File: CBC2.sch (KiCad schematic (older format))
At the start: 204 parts, among them K0:0 KEYSW, K0:1 KEYSW, K0:10 KEYSW, K0:11 KEYSW, K0:12 KEYSW, K0:13 KEYSW, K0:14 KEYSW, K0:15 KEYSW, K0:16 KEYSW, K0:2 KEYSW, K0:3 KEYSW, K0:4 KEYSW, K0:5 KEYSW, K0:6 KEYSW, K0:7 KEYSW, K0:8 KEYSW, K0:9 KEYSW, K0:? KEYSW, U1 Teensy2.0++

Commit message: finished schematics
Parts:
- added C1, C2: 0.1u, symbol Device:C
- added LED1, LED2, LED3: LED, symbol Device:LED
- added LED_R1, LED_R2, LED_R3, R2: 1k, symbol Device:R
- added R1: 10k, symbol Device:R
- added SW1: SW_Push, symbol Switch:SW_Push
- D0:0, D0:1, D0:11, D0:12, D0:13, D0:14, D0:15, D0:16, D0:17, D0:2, D0:3, D0:4, D0:5, D0:6, D0:7, D0:8, D0:9: symbol keyboard_parts:D -> CBC2-rescue:D-keyboard_parts
- D0:10: renamed from D0:11; symbol keyboard_parts:D -> CBC2-rescue:D-keyboard_parts
- D1:0, D1:1, D1:10, D1:11, D1:12, D1:13, D1:14, D1:15, D1:16, D1:17, D1:2, D1:3, D1:4, D1:5, D1:6, D1:7, D1:8, D1:9, D2:0, D2:1, D2:10, D2:11, D2:12, D2:13, D2:14, D2:15, D2:16, D2:17, D2:2, D2:3, D2:4, D2:5, D2:6, D2:7, D2:8, D2:9, D3:0, D3:1, D3:10, D3:11, D3:12, D3:14, D3:15, D3:16, D3:17, D3:2, D3:3, D3:4, D3:5, D3:6, D3:7, D3:8, D3:9, D4:0, D4:1, D4:10, D4:11, D4:14, D4:15, D4:16, D4:17, D4:2, D4:3, D4:4, D4:5, D4:6, D4:7, D4:8, D4:9, D5:0, D5:1, D5:10, D5:12, D5:13, D5:14, D5:15, D5:16, D5:2, D5:5, D5:9: renamed from D0:?; symbol keyboard_parts:D -> CBC2-rescue:D-keyboard_parts
- K0:0, K0:1, K0:10, K0:11, K0:12, K0:13, K0:14, K0:15, K0:16, K0:2, K0:3, K0:4, K0:5, K0:6, K0:7, K0:8, K0:9: symbol keyboard_parts:KEYSW -> CBC2-rescue:KEYSW-keyboard_parts
- K1:0, K1:1, K1:10, K1:11, K1:12, K1:13, K1:14, K1:15, K1:16, K1:17, K1:2, K1:3, K1:4, K1:5, K1:6, K1:7, K1:8, K1:9, K2:0, K2:1, K2:10, K2:11, K2:12, K2:13, K2:14, K2:15, K2:16, K2:17, K2:2, K2:3, K2:4, K2:5, K2:6, K2:7, K2:8, K2:9, K3:0, K3:1, K3:10, K3:11, K3:12, K3:14, K3:15, K3:16, K3:17, K3:2, K3:3, K3:4, K3:5, K3:6, K3:7, K3:8, K3:9, K4:0, K4:1, K4:10, K4:11, K4:13, K4:14, K4:15, K4:16, K4:17, K4:2, K4:3, K4:4, K4:5, K4:6, K4:7, K4:8, K4:9, K5:0, K5:1, K5:10, K5:12, K5:13, K5:14, K5:15, K5:16, K5:2, K5:5, K5:9: renamed from K0:?; symbol keyboard_parts:KEYSW -> CBC2-rescue:KEYSW-keyboard_parts
- U1: symbol keyboard_parts:Teensy2.0++ -> CBC2-rescue:Teensy2.0++-keyboard_parts
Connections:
- net labels added: VCC, led1, led2, led3
- wire segments 203 -> 208
- no-connect marks 0 -> 19
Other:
- note removed: "TODO: VCC capacitors, reset button, ALE needs 1k resistor to GND, PC4 PC5 PC6 are leds, connect rows + cols"
- moved on the sheet: C_REF1

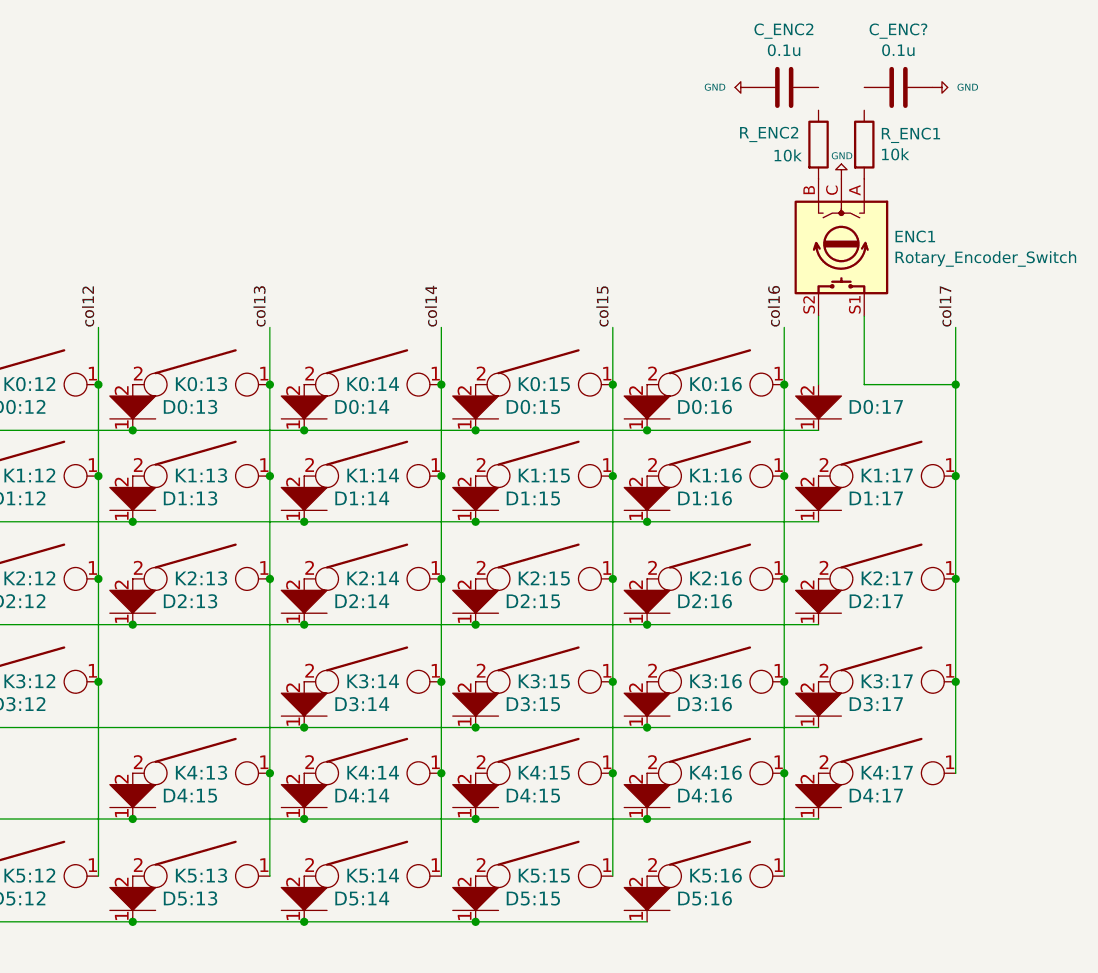
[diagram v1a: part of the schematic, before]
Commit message: started pcb layout. teensy footprint needs adjustments, or install teensy library and replace symbol
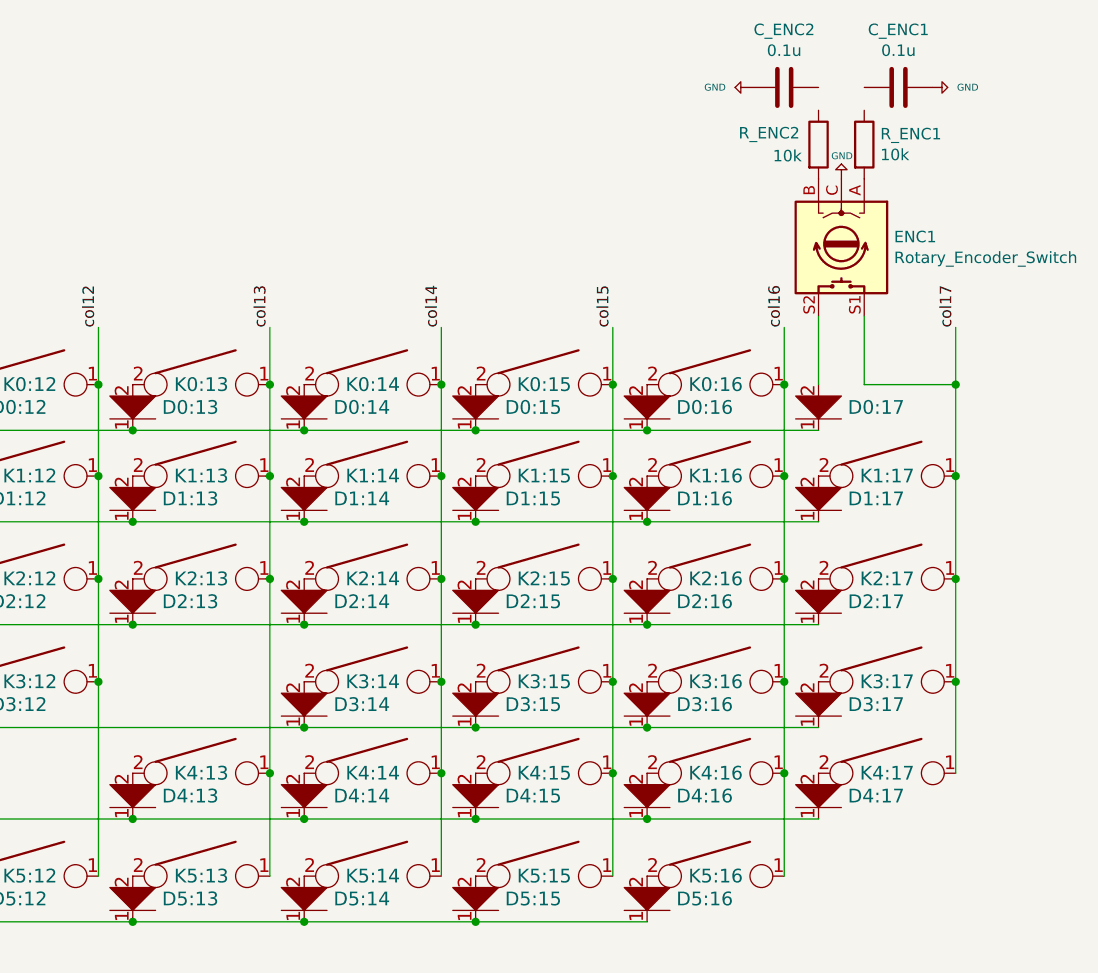
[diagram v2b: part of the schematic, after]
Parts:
- C1, C2, C_ENC2, C_REF1: footprint (none) -> Capacitor_THT:C_Axial_L3.8mm_D2.6mm_P7.50mm_Horizontal
- C_ENC1: renamed from C_ENC?; footprint (none) -> Capacitor_THT:C_Axial_L3.8mm_D2.6mm_P7.50mm_Horizontal
- D0:0, D0:1, D0:10, D0:11, D0:12, D0:13, D0:14, D0:15, D0:16, D0:17, D0:2, D0:3, D0:4, D0:5, D0:6, D0:7, D0:8, D0:9, D1:0, D1:1, D1:10, D1:11, D1:12, D1:13, D1:14, D1:15, D1:16, D1:17, D1:2, D1:3, D1:4, D1:5, D1:6, D1:7, D1:8, D1:9, D2:0, D2:1, D2:10, D2:11, D2:12, D2:13, D2:14, D2:15, D2:16, D2:17, D2:2, D2:3, D2:4, D2:5, D2:6, D2:7, D2:8, D2:9, D3:0, D3:1, D3:10, D3:11, D3:12, D3:14, D3:15, D3:16, D3:17, D3:2, D3:3, D3:4, D3:5, D3:6, D3:7, D3:8, D3:9, D4:0, D4:1, D4:10, D4:11, D4:14, D4:15, D4:16, D4:17, D4:2, D4:3, D4:4, D4:5, D4:6, D4:7, D4:8, D4:9, D5:0, D5:1, D5:10, D5:12, D5:13, D5:14, D5:15, D5:16, D5:2, D5:5, D5:9: footprint (none) -> keyboard_parts:D_SOD123_axial
- D4:13: renamed from D4:15; footprint (none) -> keyboard_parts:D_SOD123_axial
- ENC1: footprint (none) -> Rotary_Encoder:RotaryEncoder_Alps_EC11E-Switch_Vertical_H20mm
- K0:0, K0:1, K0:10, K0:11, K0:12, K0:13, K0:14, K0:15, K0:16, K0:2, K0:3, K0:4, K0:5, K0:6, K0:7, K0:8, K0:9, K1:0, K1:1, K1:10, K1:11, K1:12, K1:13, K1:14, K1:15, K1:16, K1:17, K1:2, K1:3, K1:4, K1:5, K1:6, K1:7, K1:8, K1:9, K2:0, K2:1, K2:10, K2:11, K2:12, K2:13, K2:14, K2:15, K2:16, K2:17, K2:2, K2:3, K2:4, K2:5, K2:6, K2:7, K2:8, K2:9, K3:0, K3:1, K3:10, K3:11, K3:12, K3:14, K3:15, K3:16, K3:17, K3:2, K3:3, K3:4, K3:5, K3:6, K3:7, K3:8, K3:9, K4:0, K4:1, K4:10, K4:11, K4:13, K4:14, K4:15, K4:16, K4:17, K4:2, K4:3, K4:4, K4:5, K4:6, K4:7, K4:8, K4:9, K5:0, K5:1, K5:10, K5:12, K5:13, K5:14, K5:15, K5:16, K5:2, K5:5, K5:9: footprint (none) -> keebs:Mx_Alps_100
- LED1, LED2, LED3: footprint (none) -> LED_THT:LED_D2.0mm_W4.0mm_H2.8mm_FlatTop
- LED_R1, LED_R2, LED_R3, R1, R2, R_ENC1, R_ENC2: footprint (none) -> Resistor_THT:R_Axial_DIN0204_L3.6mm_D1.6mm_P5.08mm_Horizontal
- SW1: footprint (none) -> Button_Switch_THT:Push_E-Switch_KS01Q01
- U1: footprint (none) -> teensy:Teensy2.0++

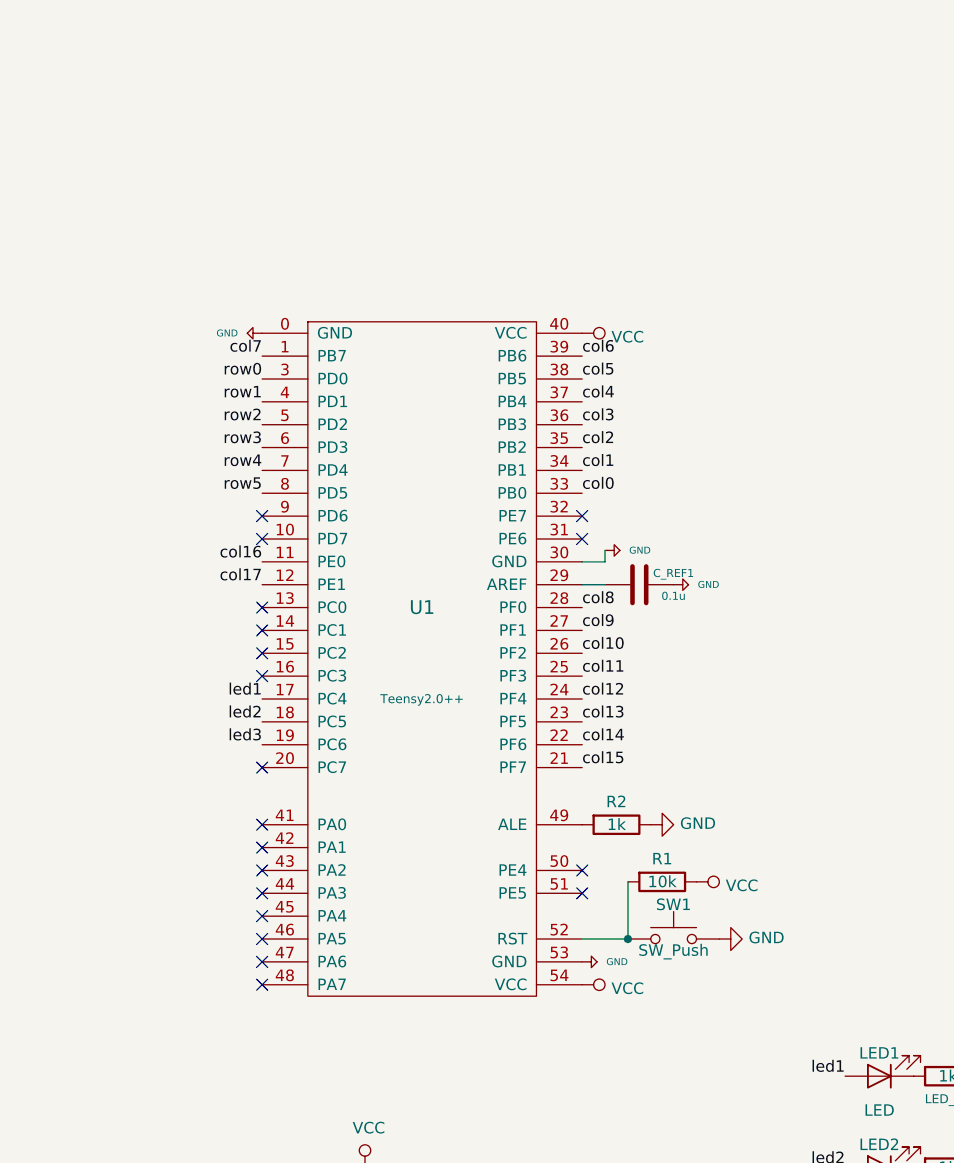
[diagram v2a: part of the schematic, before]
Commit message: added teensy symbol library to replace broken symbol and remapped connections
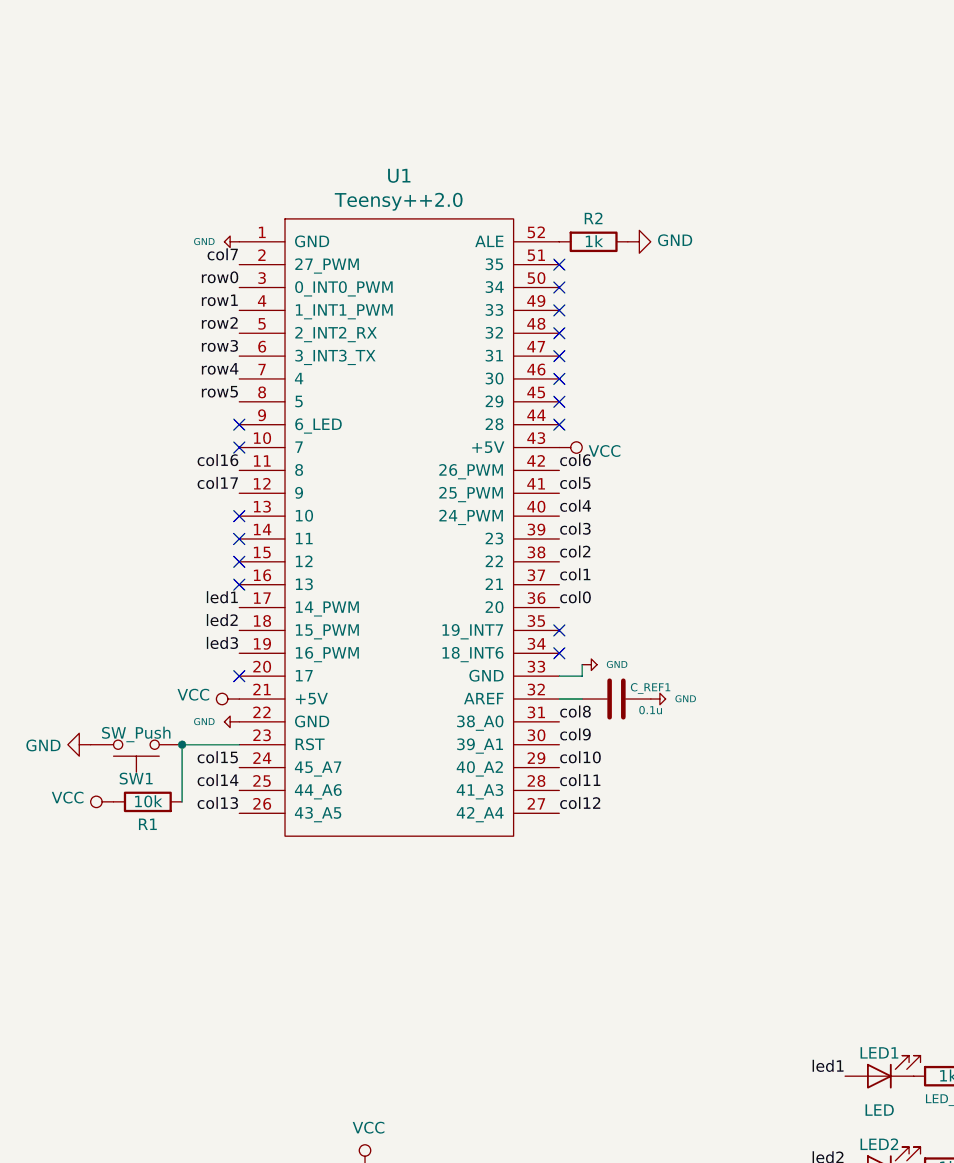
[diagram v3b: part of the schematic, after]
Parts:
- removed U1: Teensy2.0++, teensy:Teensy2.0++, symbol CBC2-rescue:Teensy2.0++-keyboard_parts
- added U1: Teensy++2.0, teensy:Teensy2.0++, symbol teensy:Teensy++2.0
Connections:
- net +5V: now also U1.1 (GND), U1.22 (GND), U1.33 (GND)
- net VCC: now also U1.21 (+5V), U1.43 (+5V)
- net col0: now also U1.36 (20)
- net col1: now also U1.37 (21)
- net col10: now also U1.29 (40_A2)
- net col11: now also U1.28 (41_A3)
- net col12: now also U1.27 (42_A4)
- net col13: now also U1.26 (43_A5)
- net col14: now also U1.25 (44_A6)
- net col15: now also U1.24 (45_A7)
- net col16: now also U1.11 (8)
- net col17: now also U1.12 (9)
- net col2: now also U1.38 (22)
- net col3: now also U1.39 (23)
- net col4: now also U1.40 (24_PWM)
- net col5: now also U1.41 (25_PWM)
- net col6: now also U1.42 (26_PWM)
- net col7: now also U1.2 (27_PWM)
- net col8: now also U1.31 (38_A0)
- net col9: now also U1.30 (39_A1)
- net led1: now also U1.17 (14_PWM)
- net led2: now also U1.18 (15_PWM)
- net led3: now also U1.19 (16_PWM)
- net row0: now also U1.3 (0_INT0_PWM)
- net row1: now also U1.4 (1_INT1_PWM)
- net row2: now also U1.5 (2_INT2_RX)
- net row3: now also U1.6 (3_INT3_TX)
- net row4: now also U1.7 (4)
- net row5: now also U1.8 (5)
- net at C_REF1.2: now also U1.32 (AREF)
- net at R2.2: now also U1.52 (ALE)
- net at R1.2, SW1.1: now also U1.23 (RST)
- no-connect marks 19 -> 17
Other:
- moved on the sheet: C_REF1, R1, R2, SW1

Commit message: switched to keeb.io library and placed diodes
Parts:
- removed D3:17, D5:2: D, keyboard_parts:D_SOD123_axial, symbol CBC2-rescue:D-keyboard_parts
- removed K3:17, K5:2: KEYSW, keebs:Mx_Alps_100, symbol CBC2-rescue:KEYSW-keyboard_parts
- D0:0: footprint keyboard_parts:D_SOD123_axial -> Keebio-Parts:Diode-dual; symbol CBC2-rescue:D-keyboard_parts -> keyboard_parts:D
- D0:1, D0:10, D0:11, D0:12, D0:13, D0:14, D0:15, D0:16, D0:17, D0:2, D0:3, D0:4, D0:5, D0:6, D0:7, D0:8, D0:9, D1:0, D1:1, D1:10, D1:11, D1:12, D1:13, D1:14, D1:15, D1:16, D1:17, D1:2, D1:3, D1:4, D1:5, D1:6, D1:7, D1:8, D1:9, D2:0, D2:1, D2:10, D2:11, D2:12, D2:13, D2:14, D2:15, D2:16, D2:17, D2:2, D2:3, D2:4, D2:5, D2:6, D2:7, D2:8, D2:9, D3:0, D3:1, D3:10, D3:11, D3:12, D3:14, D3:15, D3:16, D3:2, D3:3, D3:4, D3:5, D3:6, D3:7, D3:8, D3:9, D4:0, D4:1, D4:10, D4:11, D4:13, D4:14, D4:15, D4:16, D4:17, D4:2, D4:3, D4:4, D4:5, D4:6, D4:7, D4:8, D4:9, D5:0, D5:1, D5:10, D5:12, D5:13, D5:14, D5:15, D5:16, D5:5, D5:9: footprint keyboard_parts:D_SOD123_axial -> Keebio-Parts:Diode-dual; symbol CBC2-rescue:D-keyboard_parts -> CBC2-rescue:D-keyboard_parts-CBC2-rescue
- K0:0: footprint keebs:Mx_Alps_100 -> Keebio-Parts:Hybrid_PCB_100H_Dual_hole-LED; symbol CBC2-rescue:KEYSW-keyboard_parts -> keyboard_parts:KEYSW
- K0:1, K0:10, K0:11, K0:12, K0:13, K0:14, K0:15, K0:16, K0:2, K0:3, K0:4, K0:5, K0:6, K0:7, K0:8, K0:9, K1:0, K1:1, K1:10, K1:11, K1:12, K1:14, K1:15, K1:16, K1:17, K1:2, K1:3, K1:4, K1:5, K1:6, K1:7, K1:8, K1:9, K2:0, K2:1, K2:10, K2:11, K2:12, K2:13, K2:14, K2:15, K2:16, K2:2, K2:3, K2:4, K2:5, K2:6, K2:7, K2:8, K2:9, K3:0, K3:1, K3:10, K3:11, K3:14, K3:15, K3:16, K3:2, K3:3, K3:4, K3:5, K3:6, K3:7, K3:8, K3:9, K4:1, K4:10, K4:13, K4:14, K4:15, K4:16, K4:2, K4:3, K4:4, K4:5, K4:6, K4:7, K4:8, K4:9, K5:0, K5:1, K5:10, K5:12, K5:13, K5:14, K5:15, K5:16, K5:9: footprint keebs:Mx_Alps_100 -> Keebio-Parts:Hybrid_PCB_100H_Dual_hole-LED; symbol CBC2-rescue:KEYSW-keyboard_parts -> CBC2-rescue:KEYSW-keyboard_parts-CBC2-rescue
- K1:13, K2:17, K3:12, K4:0, K4:11, K4:17: footprint keebs:Mx_Alps_100 -> Keebio-Parts:Hybrid_PCB_200H-dual-LED; symbol CBC2-rescue:KEYSW-keyboard_parts -> CBC2-rescue:KEYSW-keyboard_parts-CBC2-rescue
- K5:5: footprint keebs:Mx_Alps_100 -> Keebio-Parts:Hybrid_PCB_625H; symbol CBC2-rescue:KEYSW-keyboard_parts -> CBC2-rescue:KEYSW-keyboard_parts-CBC2-rescue
- SW1: footprint Button_Switch_THT:Push_E-Switch_KS01Q01 -> Keebio-Parts:SW_Tactile_SPST_Angled_MJTP1117
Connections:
- net at R_ENC2.1: now also C_ENC2.1
- net at R_ENC1.1: now also C_ENC1.2

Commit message: fixed +5v vs GND discrepency. More routing.
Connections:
- net +5V is gone; now on net GND: C_ENC1.1, C_ENC2.2, C_REF1.1, ENC1.C, U1.1 (GND), U1.22 (GND), U1.33 (GND)
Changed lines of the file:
@@
 $EndComp
 $Comp
-L CBC2-rescue:GND-keyboard_parts-CBC2-rescue #PWR0101
+L power:GND #PWR0101
 U 1 1 5CB6F7E9
 P 19750 1650
@@
 $EndComp
 $Comp
-L CBC2-rescue:GND-keyboard_parts-CBC2-rescue #PWR0102
+L power:GND #PWR0102
 U 1 1 5CB6FBB8
 P 18950 1650
@@
 $EndComp
 $Comp
-L CBC2-rescue:GND-keyboard_parts-CBC2-rescue #PWR0103
+L power:GND #PWR0103
 U 1 1 5CB7113D
 P 19350 2050
@@
 col17
 $Comp
-L CBC2-rescue:GND-keyboard_parts-CBC2-rescue #PWR0104
+L power:GND #PWR0104
 U 1 1 5D09CE0D
 P 4250 4800
@@
 $EndComp
 $Comp
-L CBC2-rescue:GND-keyboard_parts-CBC2-rescue #PWR0105
-U 1 1 5D0A1009
-P 2450 2800
-F 0 "#PWR0105" H 2450 2850 20  0001 C CNN
-F 1 "GND" V 2450 2600 30  0000 L CNN
-F 2 "" H 2450 2800 60  0000 C CNN
-F 3 "" H 2450 2800 60  0000 C CNN
-	1    2450 2800
-	0    1    1    0
-$EndComp
-$Comp
-L CBC2-rescue:GND-keyboard_parts-CBC2-rescue #PWR0106
+L power:GND #PWR0106
 U 1 1 5D0A271E
 P 2450 4900
@@
 $EndComp
 $Comp
-L CBC2-rescue:GND-keyboard_parts-CBC2-rescue #PWR0107
+L power:GND #PWR0107
 U 1 1 5D0A3A4B
 P 3950 4650
@@
 	0    -1   -1   0
 $EndComp
-$Comp
-L teensy:Teensy++2.0 U1
-U 1 1 5CB69812
-P 3150 3950
-F 0 "U1" H 3150 5387 60  0000 C CNN
-F 1 "Teensy++2.0" H 3150 5281 60  0000 C CNN
-F 2 "teensy:Teensy2.0++" H 3250 3100 60  0001 C CNN
-F 3 "" H 3250 3100 60  0000 C CNN
-	1    3150 3950
-	1    0    0    -1
-$EndComp
 Text Label 3850 5300 0    50   ~ 0
 col12
@@
 	19450 1650 19450 1750
 Connection ~ 19450 1650
+$Comp
+L teensy:Teensy++2.0 U1
+U 1 1 5CB69812
+P 3150 3950
+F 0 "U1" H 3150 5387 60  0000 C CNN
+F 1 "Teensy++2.0" H 3150 5281 60  0000 C CNN
+F 2 "teensy:Teensy2.0++" H 3250 3100 60  0001 C CNN
+F 3 "" H 3250 3100 60  0000 C CNN
+	1    3150 3950
+	1    0    0    -1
+$EndComp
+$Comp
+L power:GND #PWR0105
+U 1 1 5CB1E288
+P 2450 2800
+F 0 "#PWR0105" H 2450 2550 50  0001 C CNN
+F 1 "GND" V 2455 2672 50  0000 R CNN
+F 2 "" H 2450 2800 50  0001 C CNN
+F 3 "" H 2450 2800 50  0001 C CNN
+	1    2450 2800
+	0    1    1    0
+$EndComp
 $EndSCHEMATC

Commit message: i lied. started the pcb from scratch after modifying schematic and layout plans
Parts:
- removed D0:16: D, Keebio-Parts:Diode-dual, symbol CBC2-rescue:D-keyboard_parts-CBC2-rescue
- removed K0:16: KEYSW, Keebio-Parts:Hybrid_PCB_100H_Dual_hole-LED, symbol CBC2-rescue:KEYSW-keyboard_parts-CBC2-rescue
- removed LED1, LED2, LED3: LED, LED_THT:LED_D2.0mm_W4.0mm_H2.8mm_FlatTop, symbol Device:LED
- removed LED_R1, LED_R2, LED_R3: 1k, Resistor_THT:R_Axial_DIN0204_L3.6mm_D1.6mm_P5.08mm_Horizontal, symbol Device:R
- added D1:18, D2:18, D3:14: D, Keebio-Parts:Diode-dual, symbol CBC2-rescue:D-keyboard_parts-CBC2-rescue
- added K1:18, K3:14: KEYSW, MX_Alps_Hybrid:MX-1U, symbol CBC2-rescue:KEYSW-keyboard_parts-CBC2-rescue
- added K2:18: KEYSW, MX_Alps_Hybrid:MX-2U, symbol CBC2-rescue:KEYSW-keyboard_parts-CBC2-rescue
- K0:0, K0:1, K0:10, K0:11, K0:12, K0:13, K0:14, K0:15, K0:2, K0:3, K0:4, K0:5, K0:6, K0:7, K0:8, K0:9, K1:0, K1:1, K1:10, K1:11, K1:12, K1:14, K1:15, K1:16, K1:17, K1:2, K1:3, K1:4, K1:5, K1:6, K1:7, K1:8, K1:9, K2:1, K2:10, K2:11, K2:12, K2:14, K2:15, K2:16, K2:2, K2:3, K2:4, K2:5, K2:6, K2:7, K2:8, K2:9, K3:1, K3:10, K3:11, K3:2, K3:3, K3:4, K3:5, K3:6, K3:7, K3:8, K3:9, K4:10, K4:2, K4:3, K4:4, K4:5, K4:6, K4:7, K4:8, K4:9: footprint Keebio-Parts:Hybrid_PCB_100H_Dual_hole-LED -> MX_Alps_Hybrid:MX-1U
- K1:13: footprint Keebio-Parts:Hybrid_PCB_200H-dual-LED -> MX_Alps_Hybrid:MX-1.75U
- K2:0, K5:0: footprint Keebio-Parts:Hybrid_PCB_100H_Dual_hole-LED -> MX_Alps_Hybrid:MX-1.5U
- K2:13: footprint Keebio-Parts:Hybrid_PCB_100H_Dual_hole-LED -> MX_Alps_Hybrid:MX-1.25U
- K2:17, K4:11: footprint Keebio-Parts:Hybrid_PCB_200H-dual-LED -> MX_Alps_Hybrid:MX-1U
- K3:0: footprint Keebio-Parts:Hybrid_PCB_100H_Dual_hole-LED -> MX_Alps_Hybrid:MX-1.75U
- K3:12: footprint Keebio-Parts:Hybrid_PCB_200H-dual-LED -> MX_Alps_Hybrid:MX-2U
- K3:15: renamed from K3:14; footprint Keebio-Parts:Hybrid_PCB_100H_Dual_hole-LED -> MX_Alps_Hybrid:MX-1U
- K3:16: renamed from K3:15; footprint Keebio-Parts:Hybrid_PCB_100H_Dual_hole-LED -> MX_Alps_Hybrid:MX-1U
- K3:17: renamed from K3:16; footprint Keebio-Parts:Hybrid_PCB_100H_Dual_hole-LED -> MX_Alps_Hybrid:MX-1U
- K4:0: footprint Keebio-Parts:Hybrid_PCB_200H-dual-LED -> MX_Alps_Hybrid:MX-2.25U
- K4:12: renamed from K4:1; footprint Keebio-Parts:Hybrid_PCB_100H_Dual_hole-LED -> MX_Alps_Hybrid:MX-2.5U
- K4:14: renamed from K4:13; footprint Keebio-Parts:Hybrid_PCB_100H_Dual_hole-LED -> MX_Alps_Hybrid:MX-1U
- K4:15: renamed from K4:14; footprint Keebio-Parts:Hybrid_PCB_100H_Dual_hole-LED -> MX_Alps_Hybrid:MX-1U
- K4:16: renamed from K4:15; footprint Keebio-Parts:Hybrid_PCB_100H_Dual_hole-LED -> MX_Alps_Hybrid:MX-1U
- K4:17: renamed from K4:16; footprint Keebio-Parts:Hybrid_PCB_100H_Dual_hole-LED -> MX_Alps_Hybrid:MX-1U
- K4:18: renamed from K4:17; footprint Keebio-Parts:Hybrid_PCB_200H-dual-LED -> MX_Alps_Hybrid:MX-2U
- K5:11: renamed from K5:9; footprint Keebio-Parts:Hybrid_PCB_100H_Dual_hole-LED -> MX_Alps_Hybrid:MX-1.5U
- K5:12: renamed from K5:10; footprint Keebio-Parts:Hybrid_PCB_100H_Dual_hole-LED -> MX_Alps_Hybrid:MX-1.5U
- K5:13: renamed from K5:12; footprint Keebio-Parts:Hybrid_PCB_100H_Dual_hole-LED -> MX_Alps_Hybrid:MX-1U
- K5:14: renamed from K5:13; footprint Keebio-Parts:Hybrid_PCB_100H_Dual_hole-LED -> MX_Alps_Hybrid:MX-1U
- K5:15: renamed from K5:14; footprint Keebio-Parts:Hybrid_PCB_100H_Dual_hole-LED -> MX_Alps_Hybrid:MX-1U
- K5:16: renamed from K5:15; footprint Keebio-Parts:Hybrid_PCB_100H_Dual_hole-LED -> MX_Alps_Hybrid:MX-1U
- K5:17: renamed from K5:16; footprint Keebio-Parts:Hybrid_PCB_100H_Dual_hole-LED -> MX_Alps_Hybrid:MX-1U
- K5:2: renamed from K5:1; footprint Keebio-Parts:Hybrid_PCB_100H_Dual_hole-LED -> MX_Alps_Hybrid:MX-1.5U
- K5:7: renamed from K5:5; footprint Keebio-Parts:Hybrid_PCB_625H -> MX_Alps_Hybrid:MX-7U
- renumbered D3:14 to D3:15, D3:15 to D3:16, D3:16 to D3:17, D4:1 to D4:12, D4:13 to D4:14, D4:14 to D4:15, D4:15 to D4:16, D4:16 to D4:17, D4:17 to D4:18, D5:9 to D5:11, D5:10 to D5:12, D5:12 to D5:13, D5:13 to D5:14, D5:14 to D5:15, D5:15 to D5:16, D5:16 to D5:17, D5:1 to D5:2, D5:5 to D5:7
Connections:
- net col1: no longer K4:12.1, K5:2.1
- net col10: no longer K5:12.1
- net col11: now also K5:11.1
- net col12: now also K4:12.1, K5:12.1; no longer K5:13.1
- net col13: now also K5:13.1; no longer K4:14.1, K5:14.1
- net col14: now also K4:14.1, K5:14.1, K3:14.1; no longer K3:15.1, K4:15.1, K5:15.1
- net col15: now also K3:15.1, K4:15.1, K5:15.1; no longer K3:16.1, K4:16.1, K5:16.1
- net col16: no longer K1:16.1, K2:16.1, K3:17.1, K4:17.1, K5:17.1
- net col17: now also K3:17.1, K4:17.1, K5:17.1; no longer K4:18.1
- net col2: now also K5:2.1
- net col5: no longer K5:7.1
- net col6: now also D5:7.2
- net col7: now also K5:7.1
- net col9: no longer K5:11.1
- net row1: now also D1:18.1
- net row2: now also D2:18.1
- net row3: now also D3:14.1
- net col18: now reaches U1.13 (10)
- net col18: now also K4:18.1, K1:18.1, K2:18.1
- net at K5:7.2: no longer D5:7.2
- net led1: no longer names the net of U1.17 (14_PWM)
- net led2: no longer names the net of U1.18 (15_PWM)
- net led3: no longer names the net of U1.19 (16_PWM)
- new net: K1:16.1, K2:16.1, K3:16.1, K4:16.1, K5:16.1
- new net: D1:18.2, K1:18.2
- new net: D2:18.2, K2:18.2
- new net: D3:14.2, K3:14.2
- no-connect marks 17 -> 19
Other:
- moved on the sheet: C_ENC1, C_ENC2, D0:0, D0:1, D0:10, D0:11, D0:12, D0:13, D0:14, D0:15, D0:17, D0:2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
